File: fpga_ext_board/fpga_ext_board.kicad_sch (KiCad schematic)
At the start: 4 parts, among them J1 165MDAC, J2 65MADC, J3 65MADC, J4 Conn_02x25_Odd_Even

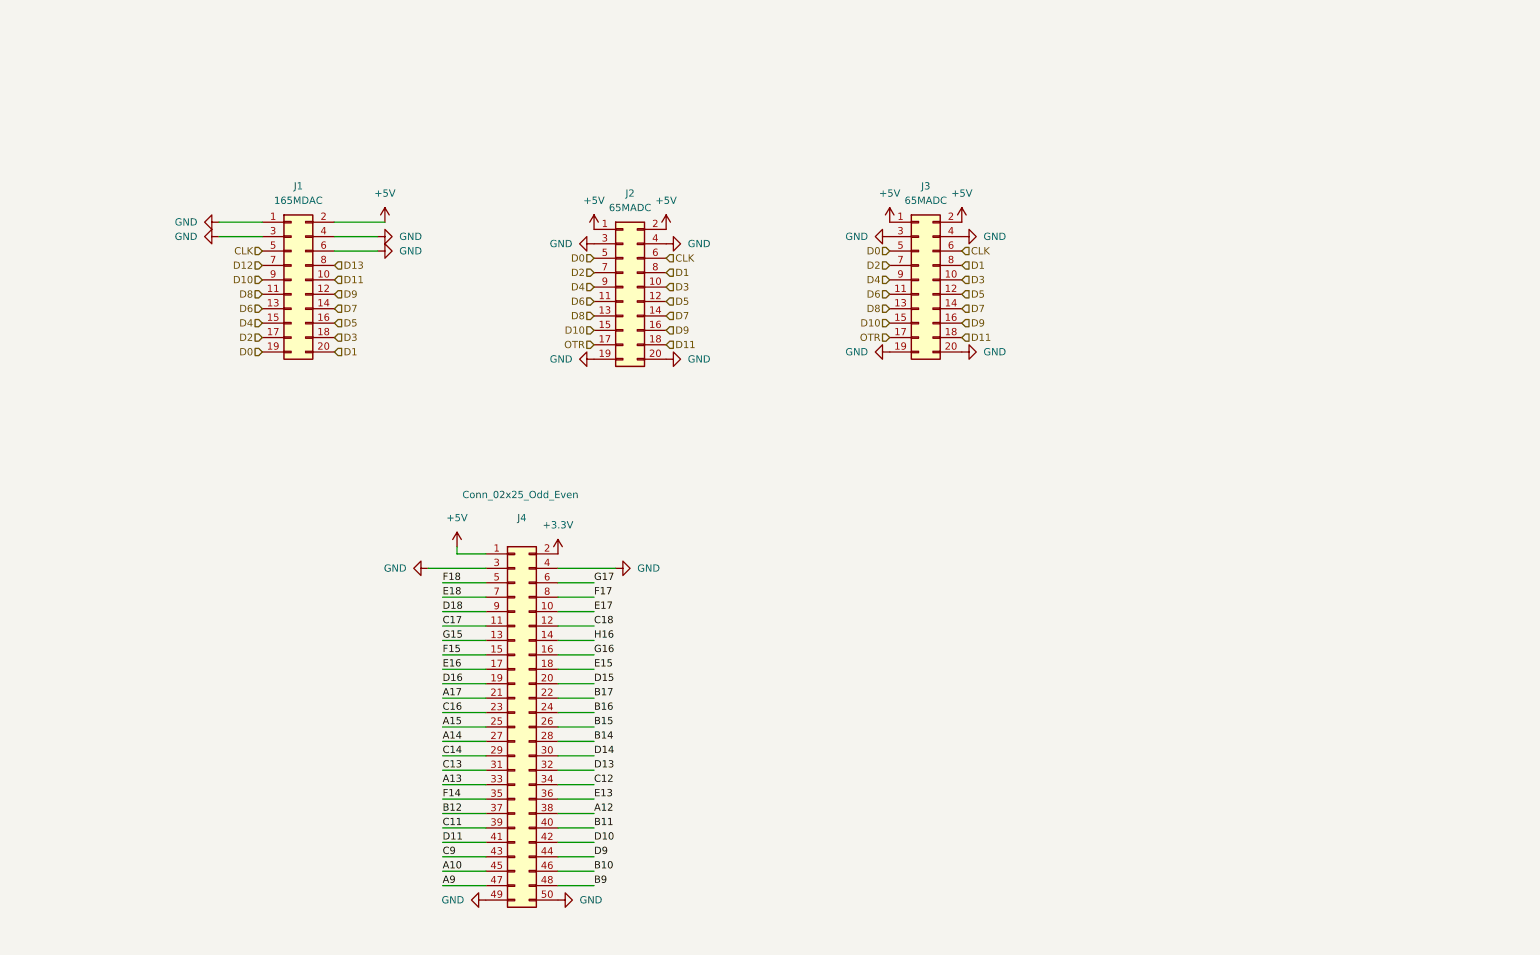
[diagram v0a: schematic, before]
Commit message: add initial version of holder
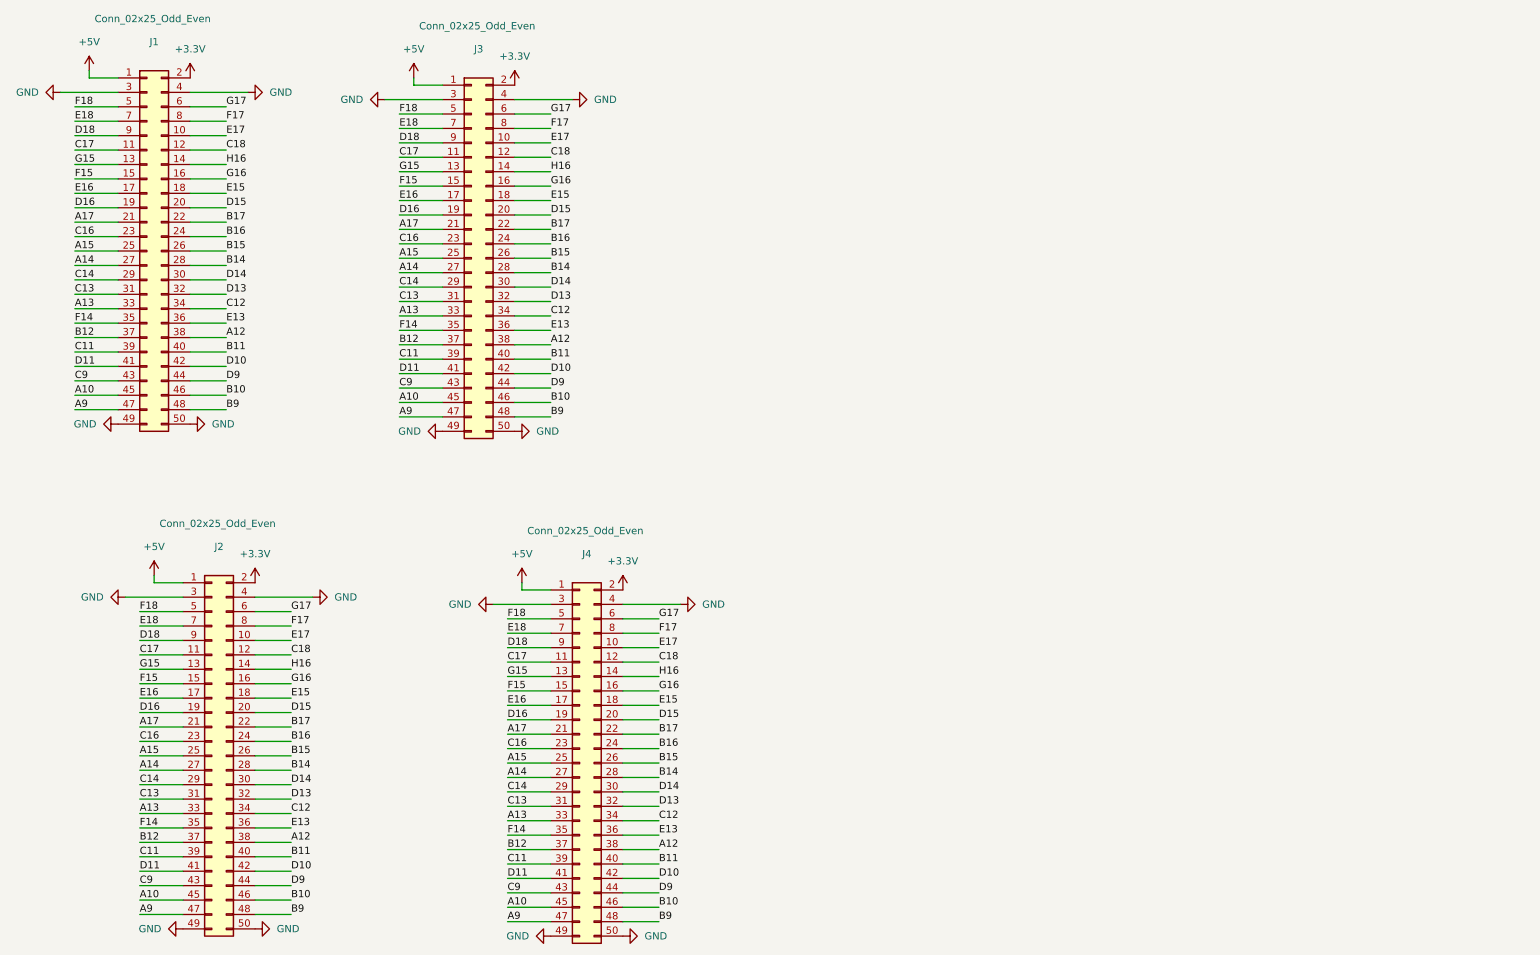
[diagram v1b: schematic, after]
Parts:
- removed J1: 165MDAC, Library:CONN-TH_DS1011-20RBSIB7-B, symbol DAC_PCB:165MDAC
- removed J2, J3: 65MADC, Library:CONN-TH_DS1011-20RBSIB7-B, symbol DAC_PCB:65MADC
- added J2, J3, J4: Conn_02x25_Odd_Even, Connector_PinSocket_2.54mm:PinSocket_2x25_P2.54mm_Vertical, symbol Connector_Generic:Conn_02x25_Odd_Even
- J1: renamed from J4; footprint (none) -> Connector_PinSocket_2.54mm:PinSocket_2x25_P2.54mm_Vertical
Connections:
- net +3.3V: now also J2.2 (Pin_2), J3.2 (Pin_2), J4.2 (Pin_2)
- net +5V: now also J2.1 (Pin_1), J3.1 (Pin_1), J4.1 (Pin_1)
- net A10: now also J2.45 (Pin_45), J3.45 (Pin_45), J4.45 (Pin_45)
- net A12: now also J2.38 (Pin_38), J3.38 (Pin_38), J4.38 (Pin_38)
- net A13: now also J2.33 (Pin_33), J3.33 (Pin_33), J4.33 (Pin_33)
- net A14: now also J2.27 (Pin_27), J3.27 (Pin_27), J4.27 (Pin_27)
- net A15: now also J2.25 (Pin_25), J3.25 (Pin_25), J4.25 (Pin_25)
- net A17: now also J2.21 (Pin_21), J3.21 (Pin_21), J4.21 (Pin_21)
- net A9: now also J2.47 (Pin_47), J3.47 (Pin_47), J4.47 (Pin_47)
- net B10: now also J2.46 (Pin_46), J3.46 (Pin_46), J4.46 (Pin_46)
- net B11: now also J2.40 (Pin_40), J3.40 (Pin_40), J4.40 (Pin_40)
- net B12: now also J2.37 (Pin_37), J3.37 (Pin_37), J4.37 (Pin_37)
- net B14: now also J2.28 (Pin_28), J3.28 (Pin_28), J4.28 (Pin_28)
- net B15: now also J2.26 (Pin_26), J3.26 (Pin_26), J4.26 (Pin_26)
- net B16: now also J2.24 (Pin_24), J3.24 (Pin_24), J4.24 (Pin_24)
- net B17: now also J2.22 (Pin_22), J3.22 (Pin_22), J4.22 (Pin_22)
- net B9: now also J2.48 (Pin_48), J3.48 (Pin_48), J4.48 (Pin_48)
- net C11: now also J2.39 (Pin_39), J3.39 (Pin_39), J4.39 (Pin_39)
- net C12: now also J2.34 (Pin_34), J3.34 (Pin_34), J4.34 (Pin_34)
- net C13: now also J2.31 (Pin_31), J3.31 (Pin_31), J4.31 (Pin_31)
- net C14: now also J2.29 (Pin_29), J3.29 (Pin_29), J4.29 (Pin_29)
- net C16: now also J2.23 (Pin_23), J3.23 (Pin_23), J4.23 (Pin_23)
- net C17: now also J2.11 (Pin_11), J3.11 (Pin_11), J4.11 (Pin_11)
- net C18: now also J2.12 (Pin_12), J3.12 (Pin_12), J4.12 (Pin_12)
- net C9: now also J2.43 (Pin_43), J3.43 (Pin_43), J4.43 (Pin_43)
- net D10: now also J2.42 (Pin_42), J3.42 (Pin_42), J4.42 (Pin_42)
- net D11: now also J2.41 (Pin_41), J3.41 (Pin_41), J4.41 (Pin_41)
- net D13: now also J2.32 (Pin_32), J3.32 (Pin_32), J4.32 (Pin_32)
- net D14: now also J2.30 (Pin_30), J3.30 (Pin_30), J4.30 (Pin_30)
- net D15: now also J2.20 (Pin_20), J3.20 (Pin_20), J4.20 (Pin_20)
- net D16: now also J2.19 (Pin_19), J3.19 (Pin_19), J4.19 (Pin_19)
- net D18: now also J2.9 (Pin_9), J3.9 (Pin_9), J4.9 (Pin_9)
- net D9: now also J2.44 (Pin_44), J3.44 (Pin_44), J4.44 (Pin_44)
- net E13: now also J2.36 (Pin_36), J3.36 (Pin_36), J4.36 (Pin_36)
- net E15: now also J2.18 (Pin_18), J3.18 (Pin_18), J4.18 (Pin_18)
- net E16: now also J2.17 (Pin_17), J3.17 (Pin_17), J4.17 (Pin_17)
- net E17: now also J2.10 (Pin_10), J3.10 (Pin_10), J4.10 (Pin_10)
- net E18: now also J2.7 (Pin_7), J3.7 (Pin_7), J4.7 (Pin_7)
- net F14: now also J2.35 (Pin_35), J3.35 (Pin_35), J4.35 (Pin_35)
- net F15: now also J2.15 (Pin_15), J3.15 (Pin_15), J4.15 (Pin_15)
- net F17: now also J2.8 (Pin_8), J3.8 (Pin_8), J4.8 (Pin_8)
- net F18: now also J2.5 (Pin_5), J3.5 (Pin_5), J4.5 (Pin_5)
- net G15: now also J2.13 (Pin_13), J3.13 (Pin_13), J4.13 (Pin_13)
- net G16: now also J2.16 (Pin_16), J3.16 (Pin_16), J4.16 (Pin_16)
- net G17: now also J2.6 (Pin_6), J3.6 (Pin_6), J4.6 (Pin_6)
- net GND: now also J2.3 (Pin_3), J2.4 (Pin_4), J2.49 (Pin_49), J2.50 (Pin_50), J3.3 (Pin_3), J3.4 (Pin_4), J3.49 (Pin_49), J3.50 (Pin_50), J4.3 (Pin_3), J4.4 (Pin_4), J4.49 (Pin_49), J4.50 (Pin_50)
- net H16: now also J2.14 (Pin_14), J3.14 (Pin_14), J4.14 (Pin_14)
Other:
- moved on the sheet: J1

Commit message: continue work
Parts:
- added J5: Conn_02x17_Odd_Even, Connector_PinHeader_2.54mm:PinHeader_2x17_P2.54mm_Vertical, symbol Connector_Generic:Conn_02x17_Odd_Even
- added J6: Conn_01x08_Pin, Connector_PinHeader_2.54mm:PinHeader_1x08_P2.54mm_Vertical, symbol Connector:Conn_01x08_Pin
- added J7: Conn_01x12_Pin, Connector_PinHeader_2.54mm:PinHeader_1x12_P2.54mm_Vertical, symbol Connector:Conn_01x12_Pin
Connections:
- net +3.3V: now also J5.23 (Pin_23), J5.26 (Pin_26), J7.10 (Pin_10)
- net +5V: now also J7.11 (Pin_11)
- net A10: no longer J1.45 (Pin_45), J2.45 (Pin_45)
- net A12: no longer J1.38 (Pin_38), J2.38 (Pin_38)
- net A13: no longer J1.33 (Pin_33), J2.33 (Pin_33)
- net A14: no longer J1.27 (Pin_27), J2.27 (Pin_27)
- net A15: no longer J1.25 (Pin_25), J2.25 (Pin_25)
- net A17: no longer J1.21 (Pin_21), J2.21 (Pin_21)
- net A9: no longer J1.47 (Pin_47), J2.47 (Pin_47)
- net B10: no longer J1.46 (Pin_46), J2.46 (Pin_46)
- net B11: no longer J1.40 (Pin_40), J2.40 (Pin_40)
- net B12: no longer J1.37 (Pin_37), J2.37 (Pin_37)
- net B14: no longer J1.28 (Pin_28), J2.28 (Pin_28)
- net B15: no longer J1.26 (Pin_26), J2.26 (Pin_26)
- net B16: no longer J1.24 (Pin_24), J2.24 (Pin_24)
- net B17: no longer J1.22 (Pin_22), J2.22 (Pin_22)
- net B9: no longer J1.48 (Pin_48), J2.48 (Pin_48)
- net C11: no longer J1.39 (Pin_39), J2.39 (Pin_39)
- net C12: no longer J1.34 (Pin_34), J2.34 (Pin_34)
- net C13: no longer J1.31 (Pin_31), J2.31 (Pin_31)
- net C14: no longer J1.29 (Pin_29), J2.29 (Pin_29)
- net C16: no longer J1.23 (Pin_23), J2.23 (Pin_23)
- net C17: no longer J1.11 (Pin_11), J2.11 (Pin_11)
- net C18: no longer J1.12 (Pin_12), J2.12 (Pin_12)
- net C9: no longer J1.43 (Pin_43), J2.43 (Pin_43)
- net D10: no longer J1.42 (Pin_42), J2.42 (Pin_42)
- net D11: no longer J1.41 (Pin_41), J2.41 (Pin_41)
- net D13: no longer J1.32 (Pin_32), J2.32 (Pin_32)
- net D14: no longer J1.30 (Pin_30), J2.30 (Pin_30)
- net D15: no longer J1.20 (Pin_20), J2.20 (Pin_20)
- net D16: no longer J1.19 (Pin_19), J2.19 (Pin_19)
- net D18: no longer J1.9 (Pin_9), J2.9 (Pin_9)
- net D9: no longer J1.44 (Pin_44), J2.44 (Pin_44)
- net E13: no longer J1.36 (Pin_36), J2.36 (Pin_36)
- net E15: no longer J1.18 (Pin_18), J2.18 (Pin_18)
- net E16: no longer J1.17 (Pin_17), J2.17 (Pin_17)
- net E17: no longer J1.10 (Pin_10), J2.10 (Pin_10)
- net E18: no longer J1.7 (Pin_7), J2.7 (Pin_7)
- net F14: no longer J1.35 (Pin_35), J2.35 (Pin_35)
- net F15: no longer J1.15 (Pin_15), J2.15 (Pin_15)
- net F17: no longer J1.8 (Pin_8), J2.8 (Pin_8)
- net F18: no longer J1.5 (Pin_5), J2.5 (Pin_5)
- net G15: no longer J1.13 (Pin_13), J2.13 (Pin_13)
- net G16: no longer J1.16 (Pin_16), J2.16 (Pin_16)
- net G17: no longer J1.6 (Pin_6), J2.6 (Pin_6)
- net GND: now also J5.25 (Pin_25), J5.28 (Pin_28), J7.12 (Pin_12)
- net H16: no longer J1.14 (Pin_14), J2.14 (Pin_14)
- new net J4: J1.42 (Pin_42), J2.42 (Pin_42), J7.4 (Pin_4)
- new net J5: J1.41 (Pin_41), J2.41 (Pin_41), J6.7 (Pin_7)
- new net J6: J1.43 (Pin_43), J2.43 (Pin_43), J6.8 (Pin_8)
- new net K1: J1.48 (Pin_48), J2.48 (Pin_48), J7.7 (Pin_7)
- new net K2: J1.47 (Pin_47), J2.47 (Pin_47), J7.9 (Pin_9)
- new net K3: J1.33 (Pin_33), J2.33 (Pin_33), J6.3 (Pin_3)
- new net K5: J1.34 (Pin_34), J2.34 (Pin_34), J5.2 (Pin_2)
- new net K6: J1.44 (Pin_44), J2.44 (Pin_44), J7.5 (Pin_5)
- new net L2: J1.45 (Pin_45), J2.45 (Pin_45), J7.8 (Pin_8)
- new net L3: J1.46 (Pin_46), J2.46 (Pin_46), J7.6 (Pin_6)
- new net L4: J1.32 (Pin_32), J2.32 (Pin_32), J5.4 (Pin_4)
- new net L5: J1.31 (Pin_31), J2.31 (Pin_31), J6.2 (Pin_2)
- new net M1: J1.40 (Pin_40), J2.40 (Pin_40), J7.3 (Pin_3)
- new net M2: J1.39 (Pin_39), J2.39 (Pin_39), J6.6 (Pin_6)
- new net M5: J1.30 (Pin_30), J2.30 (Pin_30), J5.6 (Pin_6)
- new net M6: J1.29 (Pin_29), J2.29 (Pin_29), J6.1 (Pin_1)
- new net N1: J1.37 (Pin_37), J2.37 (Pin_37), J6.5 (Pin_5)
- new net N2: J1.38 (Pin_38), J2.38 (Pin_38), J7.2 (Pin_2)
- new net N4: J1.27 (Pin_27), J2.27 (Pin_27), J5.1 (Pin_1)
- new net P1: J1.35 (Pin_35), J2.35 (Pin_35), J6.4 (Pin_4)
- new net P3: J1.28 (Pin_28), J2.28 (Pin_28), J5.8 (Pin_8)
- new net P4: J1.23 (Pin_23), J2.23 (Pin_23), J5.5 (Pin_5)
- new net R1: J1.36 (Pin_36), J2.36 (Pin_36), J7.1 (Pin_1)
- new net R3: J1.25 (Pin_25), J2.25 (Pin_25), J5.3 (Pin_3)
- new net R5: J1.13 (Pin_13), J2.13 (Pin_13), J5.15 (Pin_15)
- new net R6: J1.11 (Pin_11), J2.11 (Pin_11), J5.17 (Pin_17)
- new net R7: J1.10 (Pin_10), J2.10 (Pin_10), J5.30 (Pin_30)
- new net T2: J1.26 (Pin_26), J2.26 (Pin_26), J5.10 (Pin_10)
- new net T3: J1.24 (Pin_24), J2.24 (Pin_24), J5.12 (Pin_12)
- new net T4: J1.14 (Pin_14), J2.14 (Pin_14), J5.22 (Pin_22)
- new net T5: J1.12 (Pin_12), J2.12 (Pin_12), J5.24 (Pin_24)
- new net T7: J1.9 (Pin_9), J2.9 (Pin_9), J5.19 (Pin_19)
- new net U1: J1.22 (Pin_22), J2.22 (Pin_22), J5.14 (Pin_14)
- new net U2: J1.21 (Pin_21), J2.21 (Pin_21), J5.7 (Pin_7)
- new net U4: J1.18 (Pin_18), J2.18 (Pin_18), J5.18 (Pin_18)
- new net U5: J1.16 (Pin_16), J2.16 (Pin_16), J5.20 (Pin_20)
- new net U6: J1.15 (Pin_15), J2.15 (Pin_15), J5.13 (Pin_13)
- new net U7: J1.7 (Pin_7), J2.7 (Pin_7), J5.29 (Pin_29)
- new net V2: J1.20 (Pin_20), J2.20 (Pin_20), J5.16 (Pin_16)
- new net V3: J1.19 (Pin_19), J2.19 (Pin_19), J5.9 (Pin_9)
- new net V4: J1.17 (Pin_17), J2.17 (Pin_17), J5.11 (Pin_11)
- new net V6: J1.8 (Pin_8), J2.8 (Pin_8), J5.32 (Pin_32)
- new net V7: J1.6 (Pin_6), J2.6 (Pin_6), J5.34 (Pin_34)
- new net V8: J1.5 (Pin_5), J2.5 (Pin_5), J5.33 (Pin_33)
- no-connect marks 0 -> 3
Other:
- note added: "Extension port"
- note added: "Keyboard"
- moved on the sheet: J2, J4

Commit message: update
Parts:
- added J8: Input, Connector_Molex:Molex_Micro-Fit_3.0_43650-0215_1x02_P3.00mm_Vertical, symbol Connector_Generic:Conn_01x02
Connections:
- net +5V: now also J8.1 (Pin_1); no longer J2.1 (Pin_1)
- net GND: now also J8.2 (Pin_2)
- net R7: now also J5.32 (Pin_32); no longer J5.30 (Pin_30)
- net T4: now also J5.24 (Pin_24); no longer J5.22 (Pin_22)
- net T5: now also J5.22 (Pin_22); no longer J5.24 (Pin_24)
- net V6: now also J5.30 (Pin_30); no longer J5.32 (Pin_32)
